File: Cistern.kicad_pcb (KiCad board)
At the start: 2 copper layers, 47 x 80 mm, 18 parts, among them J1 GPIO, J2 Gauge Stepper, J3 Power Connector, J4 GND, Q1 BD244C, SW1 WiFi reset, U1 ULN2003A, U3 Boost Converter (5->20 V)

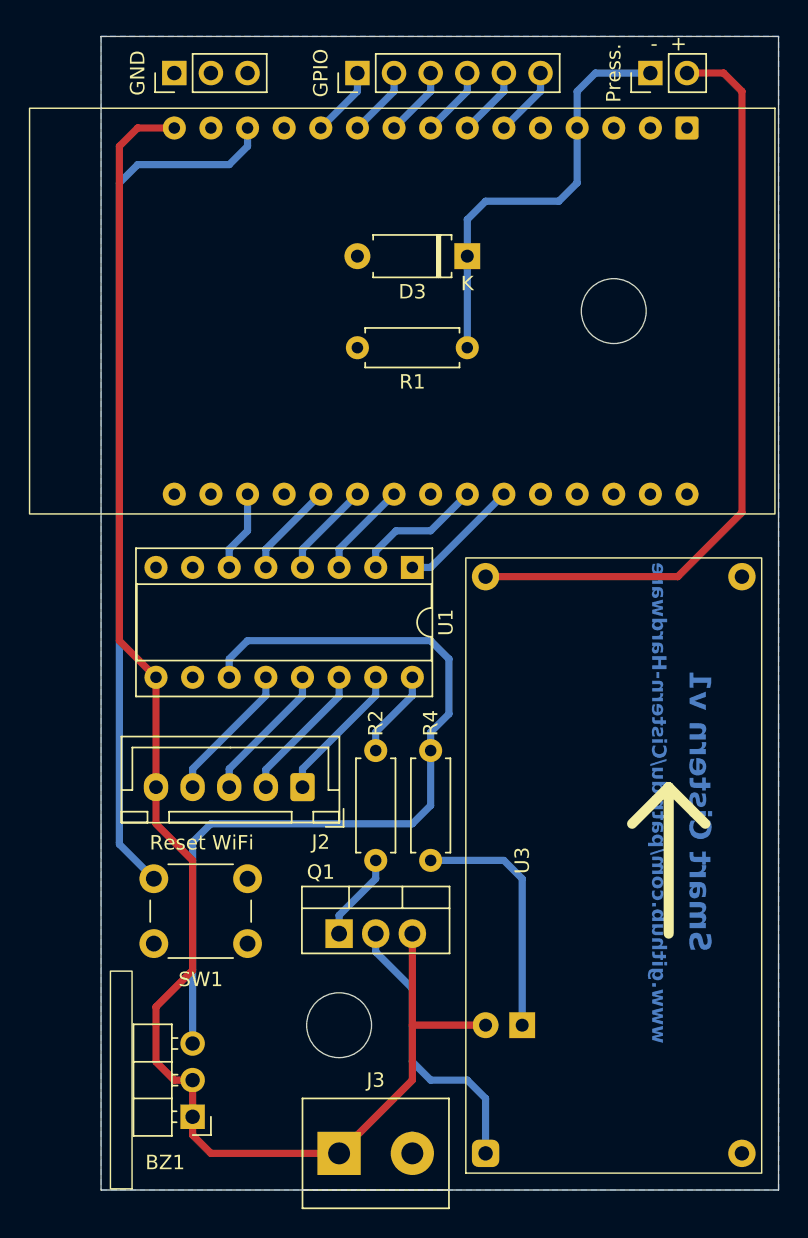
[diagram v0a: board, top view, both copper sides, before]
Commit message: Rounding corners, improving GND plane and buzzer placement
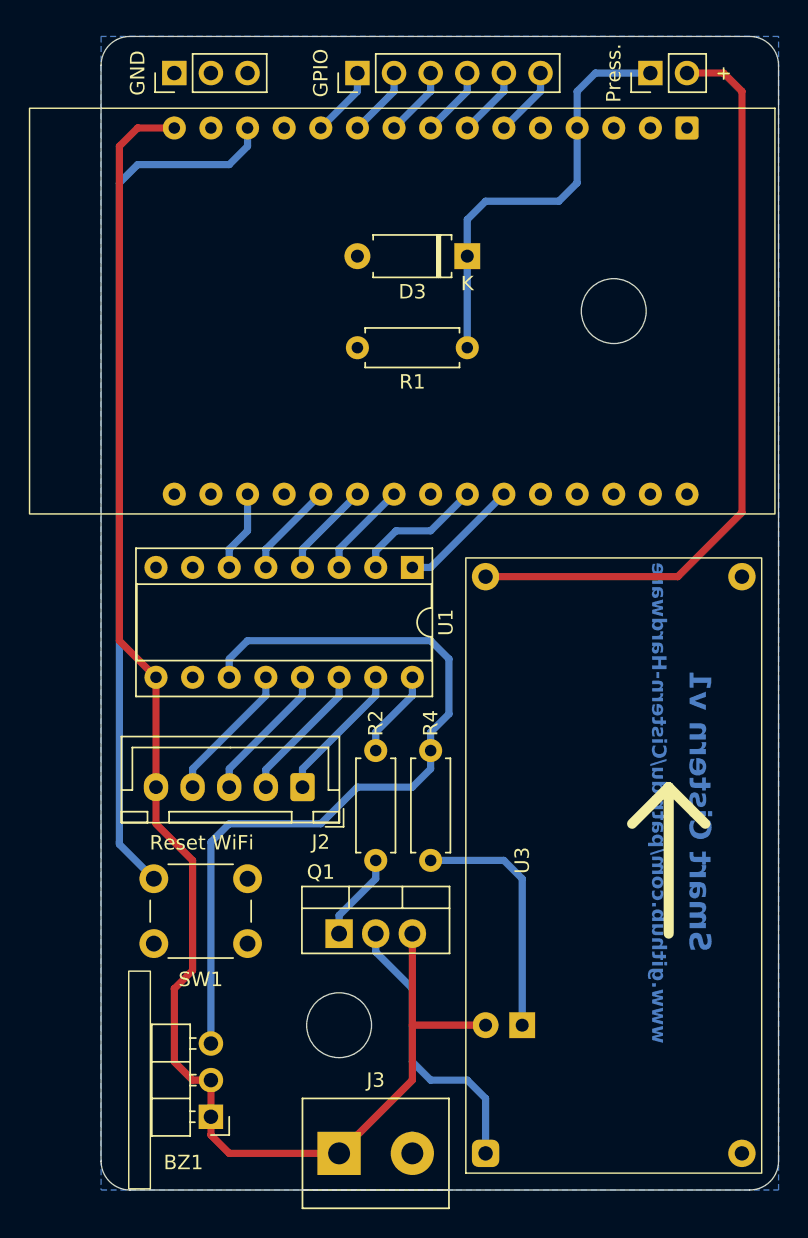
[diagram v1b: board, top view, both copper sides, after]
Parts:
- moved BZ1 1.27 mm to (92.7, 119.4)
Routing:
- net Net-(BZ1--): track 59.8 -> 57.0 mm
- net +5V: track 111.0 -> 109.2 mm
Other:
- outline, holes or cut-outs redrawn
- board text added: "+"
- board text removed: "- +"

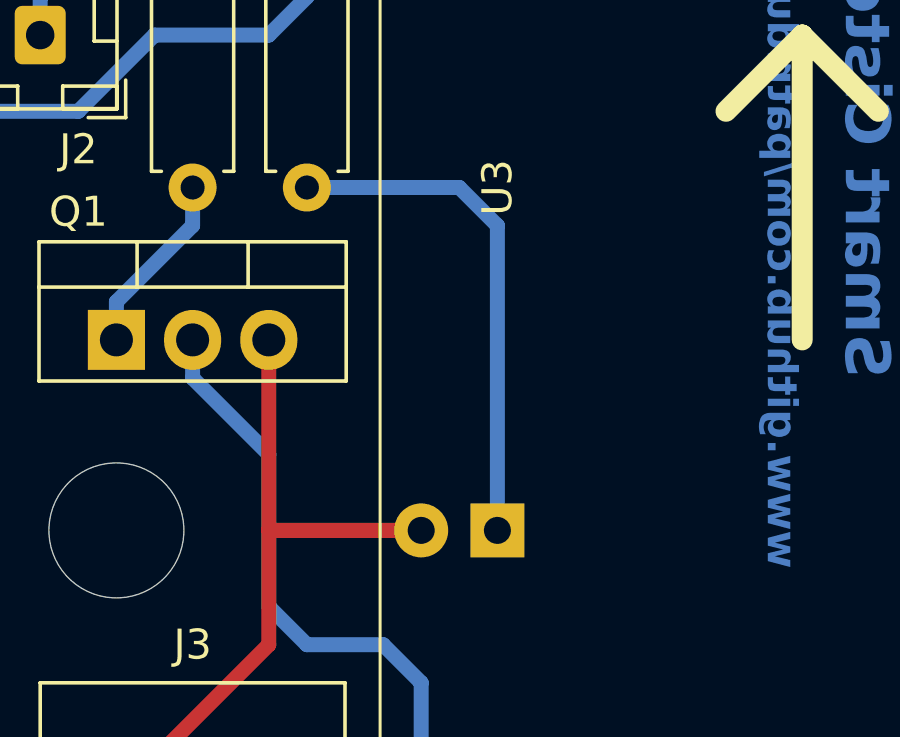
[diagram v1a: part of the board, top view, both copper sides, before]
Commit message: Fine-tuning LED position
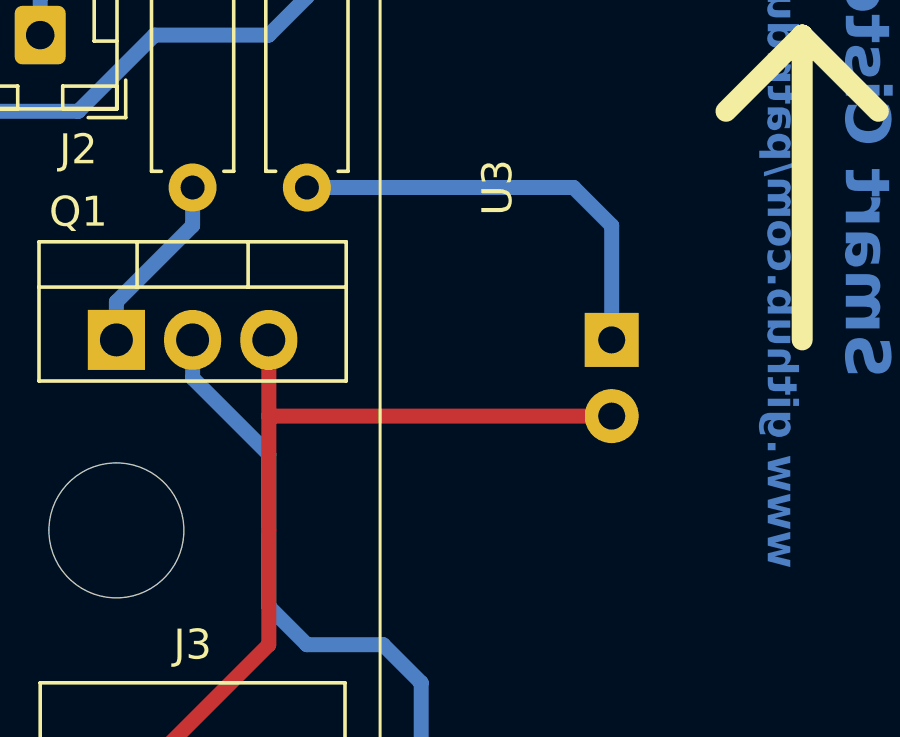
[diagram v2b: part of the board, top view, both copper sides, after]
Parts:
- moved D1 7.41 mm to (118.1, 106.7), turned to -90 degrees
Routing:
- net +5V: track 109.2 -> 115.5 mm
- net Net-(D1-K): track 17.0 -> 14.5 mm
